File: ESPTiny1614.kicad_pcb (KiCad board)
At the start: 2 copper layers, 33 x 23.9 mm, 22 parts, among them J1 Conn_01x10_Male, J2 Conn_01x10_Male, J3 Conn_01x04_Male, U1 ESP-01v090, U2 ATtiny1614-SS, U3 MCP1700-3302E_TO92

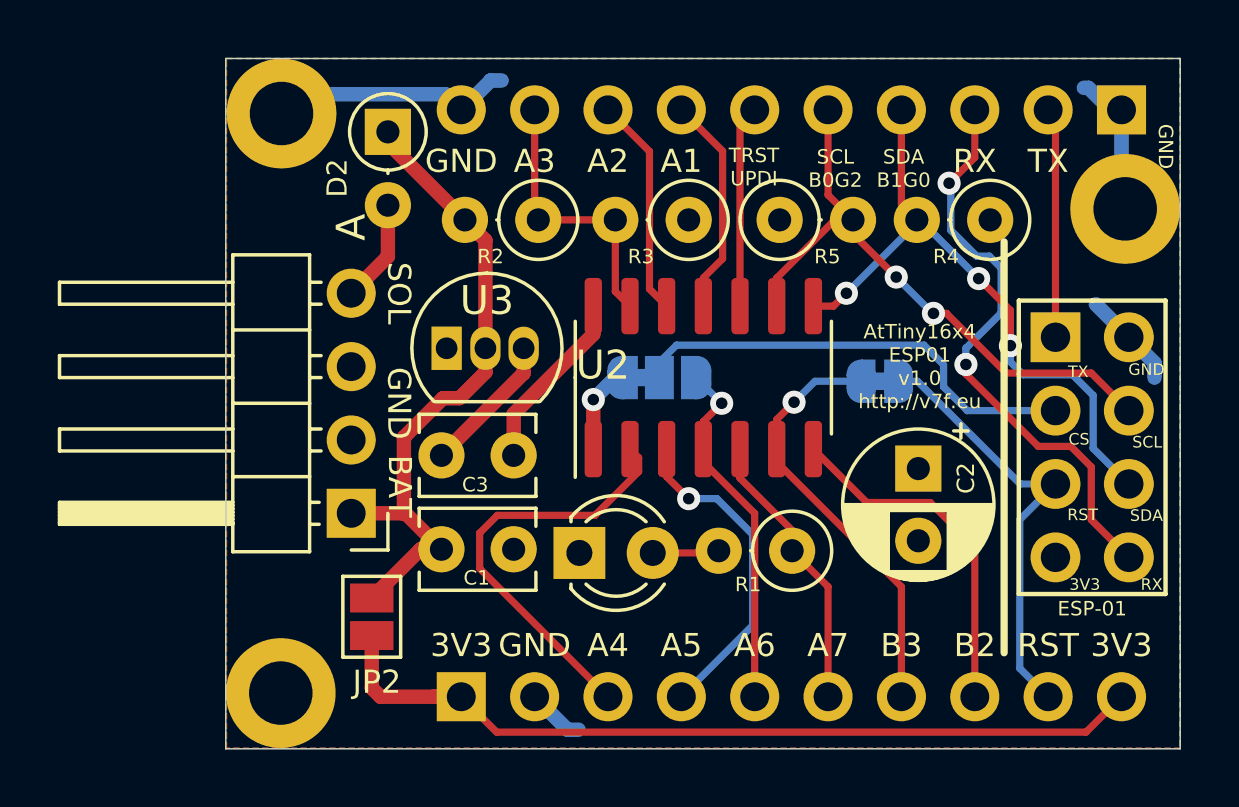
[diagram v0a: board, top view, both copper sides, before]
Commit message: Update 16x2 PCB silk, 1.0 production
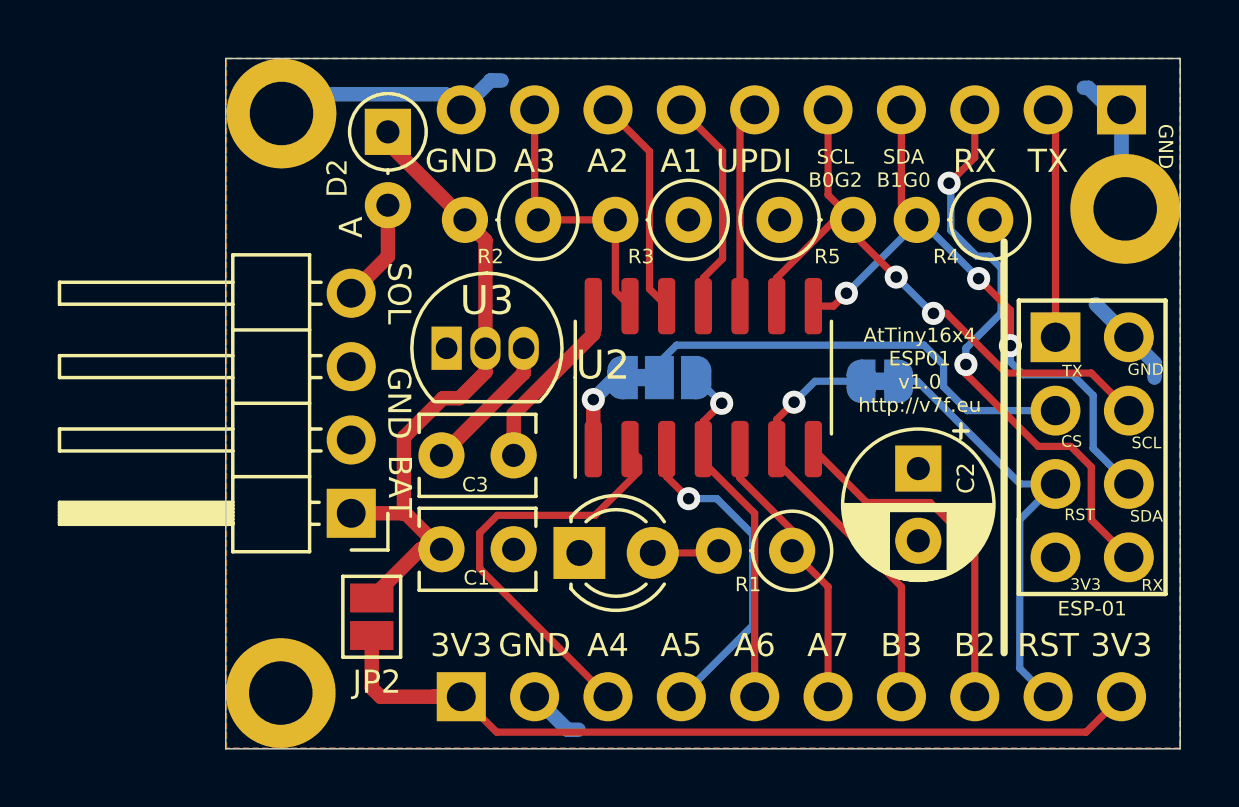
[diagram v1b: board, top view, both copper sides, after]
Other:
- board text added: "UPDI"
- board text removed: "B0"
- board text removed: "B1"
- board text removed: "SDA A6G0"
- board text removed: "Tiny RST"

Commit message: Version 2.0 Add crystal and move ESP reset to other pin
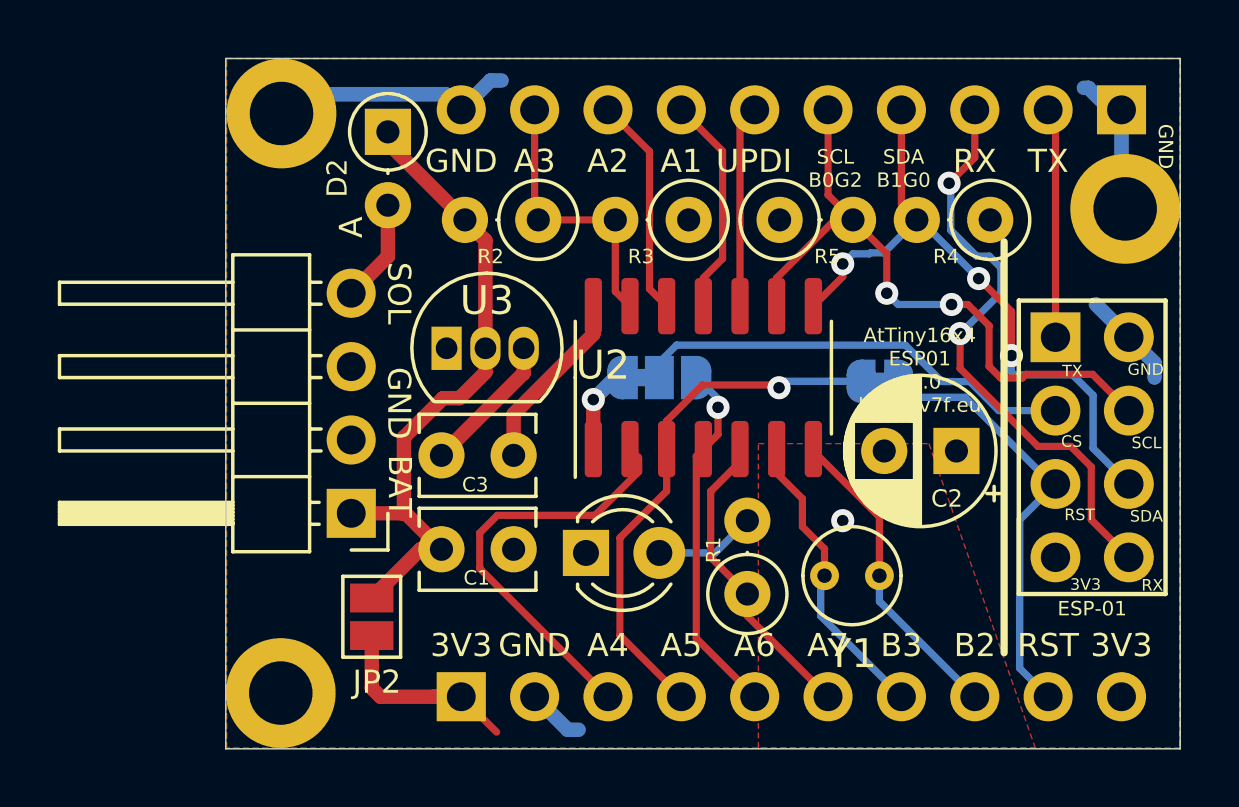
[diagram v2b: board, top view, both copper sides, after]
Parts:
- added Y1: Crystal 32.768kHz, Crystal:Crystal_Round_D3.0mm_Vertical, F.Cu at (61.7, 58.3)
- moved R1 2.16 mm to (57.1, 58.9), turned to 90 degrees
- moved C2 1.45 mm to (64.4, 54.0), turned to 180 degrees
- moved D1 0.23 mm to (51.6, 57.5)
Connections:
- JP1 pad 1: /B3 -> /A5
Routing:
- net +3V3: track 39.1 -> 16.9 mm
- net /A5: track 11.4 -> 18.5 mm
- net /B3: track 14.9 -> 10.5 mm, vias 1 -> 0
- net /SCL-B0: track 21.2 -> 22.6 mm
- net Net-(D1-Pad2): track 2.32 -> 3.74 mm
- net /A7: track 9.84 -> 11.2 mm
- net /B2: track 12.2 -> 10.9 mm
- net /A6: track 12.4 -> 13.0 mm
- net GND: vias 0 -> 1
- added copper zone on F.Cu, net GND

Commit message: Silk screen
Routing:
- net +3V3: track 16.9 -> 15.2 mm
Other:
- board text added: "AtTiny16x4"
- board text added: "v1.0 www.v7f.eu"
- board text removed: "AtTiny16x4 ESP01 v1.0 http://v7f.eu"

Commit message: Silk screen
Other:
- board text added: "v2.0 www.v7f.eu"
- board text removed: "v1.0 www.v7f.eu"
